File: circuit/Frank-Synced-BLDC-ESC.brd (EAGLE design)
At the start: 49.5 x 25.4 mm, 57 parts, among them IC1 Vreg +5V, Q1 PMOS-DPAK, Q2 NMOS-DPAK, Q4 PMOS-DPAK, Q5 NMOS-DPAK, Q7 PMOS-DPAK, Q8 NMOS-DPAK, U1 ATMEGA168MLF, U2 OSC-16MHz

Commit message: some more fine tunin' traces
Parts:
- moved C2 1.91 mm to (4.45, 20.1)
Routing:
- net N$21: track 0.66 -> 3.42 mm
- net 5V: track 69.7 -> 71.6 mm, vias 6 -> 7
- net GND: vias 24 -> 25
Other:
- board text added: "+5V"

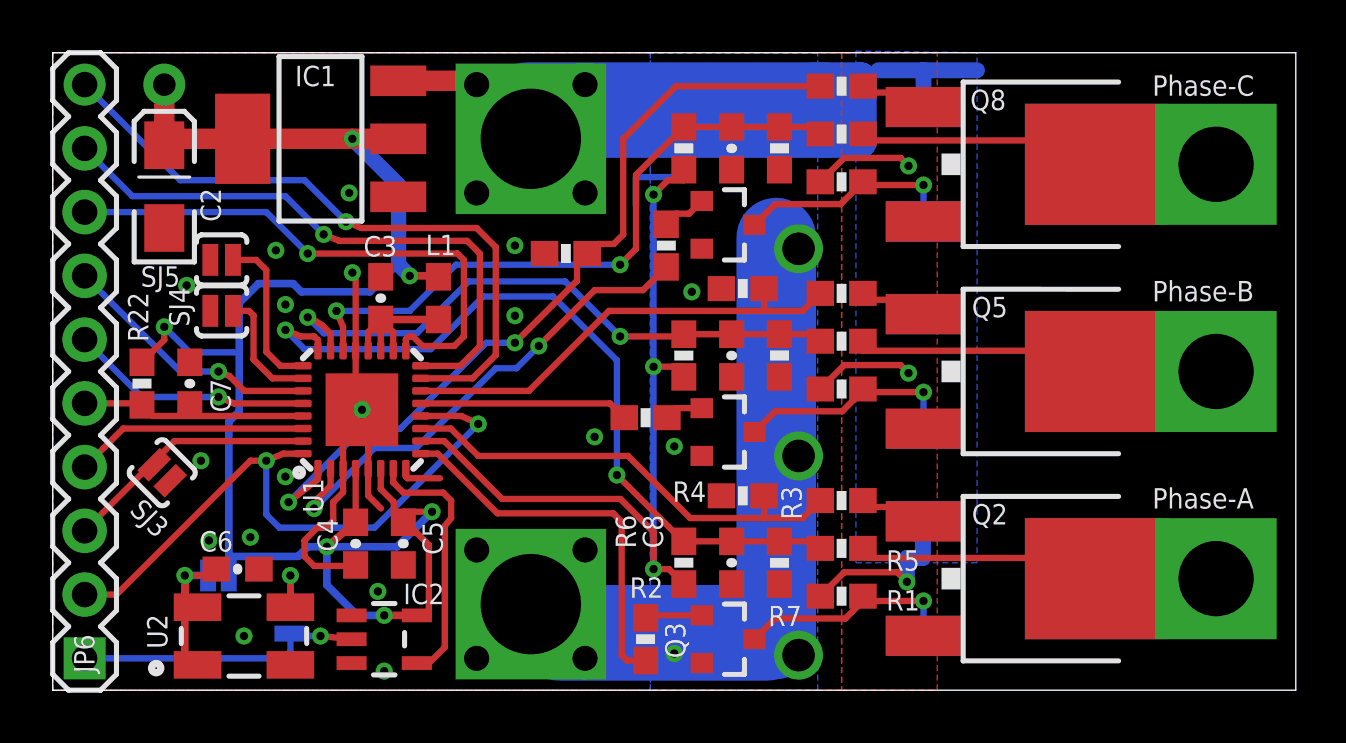
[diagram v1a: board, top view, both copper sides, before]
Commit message: just a bit more shorter, 1.9" now
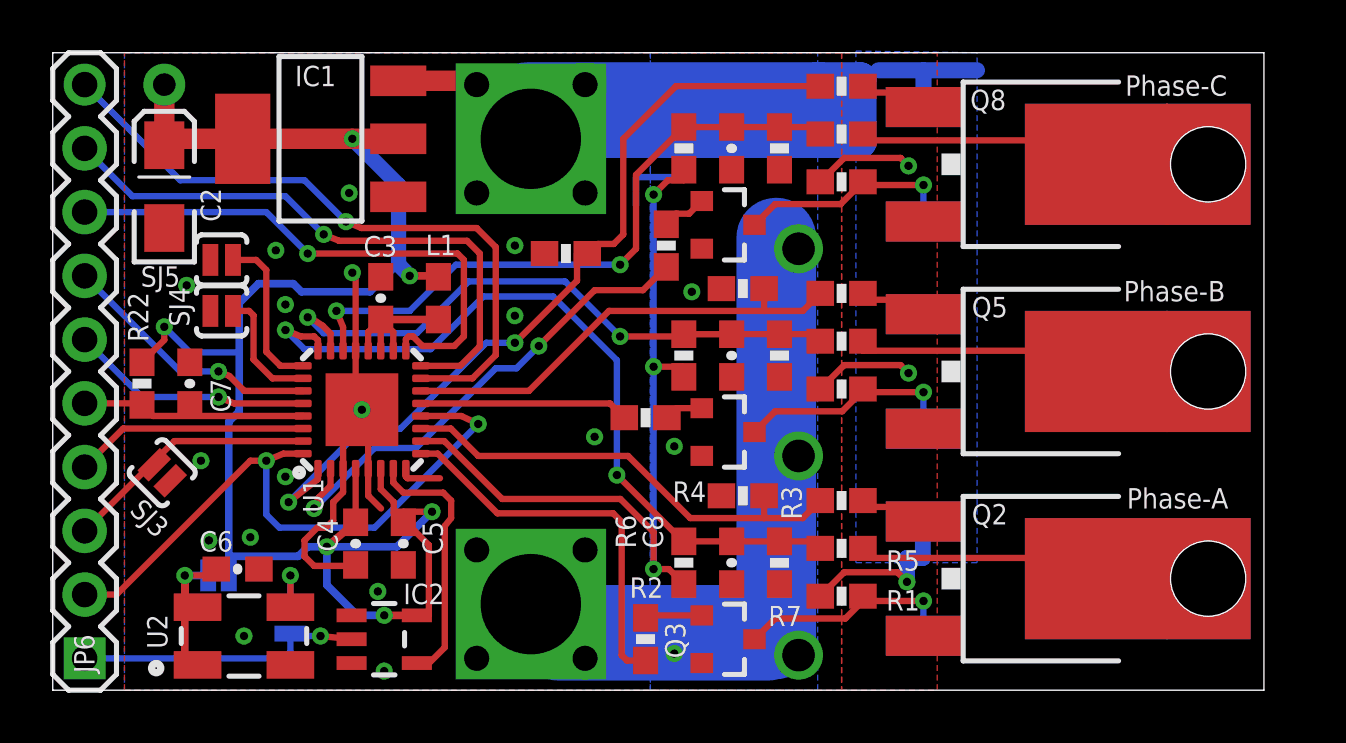
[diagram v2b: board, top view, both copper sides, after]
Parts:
- moved JP1 0.32 mm to (46.0, 4.45), turned to 270 degrees
- moved JP2 0.32 mm to (46.0, 12.7), turned to 270 degrees
- moved JP3 0.32 mm to (46.0, 21.0), turned to 270 degrees
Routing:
- net N$8: track 20.0 -> 19.4 mm
- net N$16: track 19.9 -> 19.3 mm
- net N$1: track 21.0 -> 20.4 mm
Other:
- board size 49.5 x 25.4 mm -> 48.3 x 25.4 mm
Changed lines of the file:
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@@
 <board>
 <plain>
-<wire x1="49.53" y1="0" x2="0" y2="0" width="0" layer="20"/>
+<wire x1="48.26" y1="0" x2="0" y2="0" width="0" layer="20"/>
 <wire x1="0" y1="0" x2="0" y2="25.4" width="0" layer="20"/>
-<wire x1="0" y1="25.4" x2="49.53" y2="25.4" width="0" layer="20"/>
-<wire x1="49.53" y1="25.4" x2="49.53" y2="0" width="0" layer="20"/>
+<wire x1="0" y1="25.4" x2="48.26" y2="25.4" width="0" layer="20"/>
+<wire x1="48.26" y1="25.4" x2="48.26" y2="0" width="0" layer="20"/>
 <rectangle x1="15.24" y1="18.161" x2="22.86" y2="25.4" layer="41"/>
 <rectangle x1="15.24" y1="18.161" x2="22.86" y2="25.4" layer="42" rot="R180"/>
 <wire x1="22.86" y1="20.955" x2="31.115" y2="20.955" width="0.254" layer="42"/>
-<text x="43.815" y="7.239" size="0.8128" layer="25" ratio="10">Phase-A</text>
-<text x="43.815" y="15.494" size="0.8128" layer="25" ratio="10">Phase-B</text>
-<text x="43.815" y="23.6855" size="0.8128" layer="25" ratio="10">Phase-C</text>
-<text x="48.895" y="15.494" size="0.8128" layer="26" ratio="10" rot="MR0">Phase-B</text>
-<text x="48.895" y="7.239" size="0.8128" layer="26" ratio="10" rot="MR0">Phase-A</text>
-<text x="48.8315" y="23.6855" size="0.8128" layer="26" ratio="10" rot="MR0">Phase-C</text>
+<text x="42.799" y="7.239" size="0.8128" layer="25" ratio="10">Phase-A</text>
+<text x="42.672" y="15.494" size="0.8128" layer="25" ratio="10">Phase-B</text>
+<text x="42.7355" y="23.6855" size="0.8128" layer="25" ratio="10">Phase-C</text>
+<text x="47.752" y="15.494" size="0.8128" layer="26" ratio="10" rot="MR0">Phase-B</text>
+<text x="47.879" y="7.239" size="0.8128" layer="26" ratio="10" rot="MR0">Phase-A</text>
+<text x="47.8155" y="23.6855" size="0.8128" layer="26" ratio="10" rot="MR0">Phase-C</text>
 <text x="20.8915" y="7.112" size="0.8128" layer="26" ratio="10" rot="MR0">Batt-Neg</text>
 <text x="21.1455" y="17.8435" size="0.8128" layer="26" ratio="10" rot="MR0">Batt-Pos</text>
@@
 </autorouter>
 <elements>
-<element name="JP1" library="Frank-Synced-BLDC-ESC" package="1X1-MOTOR" value="PHASE-A" x="46.355" y="4.445" smashed="yes" rot="MR90"/>
+<element name="JP1" library="Frank-Synced-BLDC-ESC" package="1X1-MOTOR" value="PHASE-A" x="46.0375" y="4.445" smashed="yes" rot="MR270"/>
 <element name="Q1" library="Frank-Synced-BLDC-ESC" package="DPAK" value="PMOS-DPAK" x="40.005" y="4.445" smashed="yes" rot="MR90">
 <attribute name="NAME" x="36.3665" y="7.112" size="0.8128" layer="26" ratio="10" rot="MR180"/>
@@
 <attribute name="VALUE" x="30.4165" y="6.4135" size="0.4064" layer="27" font="vector"/>
 </element>
-<element name="JP2" library="Frank-Synced-BLDC-ESC" package="1X1-MOTOR" value="PHASE-B" x="46.355" y="12.7" smashed="yes" rot="MR0"/>
+<element name="JP2" library="Frank-Synced-BLDC-ESC" package="1X1-MOTOR" value="PHASE-B" x="46.0375" y="12.7" smashed="yes" rot="MR270"/>
 <element name="Q4" library="Frank-Synced-BLDC-ESC" package="DPAK" value="PMOS-DPAK" x="40.005" y="12.7" smashed="yes" rot="MR90">
 <attribute name="NAME" x="36.43" y="15.4305" size="0.8128" layer="26" ratio="10" rot="MR180"/>
@@
 <attribute name="VALUE" x="30.4165" y="14.6685" size="0.4064" layer="27" font="vector"/>
 </element>
-<element name="JP3" library="Frank-Synced-BLDC-ESC" package="1X1-MOTOR" value="PHASE-C" x="46.355" y="20.955" smashed="yes" rot="MR0"/>
+<element name="JP3" library="Frank-Synced-BLDC-ESC" package="1X1-MOTOR" value="PHASE-C" x="46.0375" y="20.955" smashed="yes" rot="MR270"/>
 <element name="Q7" library="Frank-Synced-BLDC-ESC" package="DPAK" value="PMOS-DPAK" x="40.005" y="20.955" smashed="yes" rot="MR90">
 <attribute name="NAME" x="36.684" y="23.749" size="0.8128" layer="26" ratio="10" rot="MR180"/>
@@
 <contactref element="JP1" pad="P$1"/>
 <contactref element="R5" pad="1"/>
-<wire x1="41.593" y1="4.445" x2="46.355" y2="4.445" width="3.175" layer="1"/>
+<wire x1="41.593" y1="4.445" x2="46.0375" y2="4.445" width="3.175" layer="1"/>
 <contactref element="Q1" pad="4"/>
-<wire x1="41.593" y1="4.445" x2="46.355" y2="4.445" width="3.175" layer="16"/>
+<wire x1="41.593" y1="4.445" x2="46.0375" y2="4.445" width="3.175" layer="16"/>
 <wire x1="32.2825" y1="5.6515" x2="32.2825" y2="5.5245" width="0.254" layer="1"/>
 <wire x1="41.593" y1="5.5245" x2="41.593" y2="4.445" width="0.254" layer="1"/>
@@
 <wire x1="32.6635" y1="5.2705" x2="41.593" y2="5.2705" width="0.254" layer="1"/>
 <wire x1="41.593" y1="5.2705" x2="41.593" y2="4.445" width="0.254" layer="1"/>
+<wire x1="41.593" y1="4.445" x2="41.593" y2="4.445" width="0" layer="19" extent="1-16"/>
 </signal>
 <signal name="+12V">
@@
 <vertex x="23.8125" y="0"/>
 <vertex x="23.8125" y="25.4"/>
-<vertex x="0" y="25.4"/>
-<vertex x="0" y="0"/>
+<vertex x="2.8575" y="25.4"/>
+<vertex x="2.8575" y="0"/>
 </polygon>
 <polygon width="0.254" layer="1" spacing="0.254" isolate="0.254">
-<vertex x="0" y="0"/>
-<vertex x="0" y="25.4"/>
+<vertex x="2.8575" y="0"/>
+<vertex x="2.8575" y="25.4"/>
 <vertex x="31.4325" y="25.4"/>
 <vertex x="31.4325" y="0"/>
@@
 <contactref element="JP2" pad="P$1"/>
 <contactref element="R10" pad="1"/>
-<wire x1="41.593" y1="12.7" x2="46.355" y2="12.7" width="3.175" layer="1"/>
+<wire x1="41.593" y1="12.7" x2="46.0375" y2="12.7" width="3.175" layer="1"/>
 <contactref element="Q4" pad="4"/>
-<wire x1="41.593" y1="12.7" x2="46.355" y2="12.7" width="3.175" layer="16"/>
+<wire x1="41.593" y1="12.7" x2="46.0375" y2="12.7" width="3.175" layer="16"/>
 <wire x1="32.2825" y1="13.9065" x2="32.2825" y2="13.5255" width="0.254" layer="1"/>
 <wire x1="32.2825" y1="13.5255" x2="41.593" y2="13.5255" width="0.254" layer="1"/>
 <wire x1="41.593" y1="13.5255" x2="41.593" y2="12.7" width="0.254" layer="1"/>
+<wire x1="41.593" y1="12.7" x2="41.593" y2="12.7" width="0" layer="19" extent="1-16"/>
 </signal>
 <signal name="N$10">
@@
 <contactref element="JP3" pad="P$1"/>
 <contactref element="R17" pad="1"/>
-<wire x1="41.593" y1="20.955" x2="46.355" y2="20.955" width="3.175" layer="1"/>
+<wire x1="41.593" y1="20.955" x2="46.0375" y2="20.955" width="3.175" layer="1"/>
 <contactref element="Q7" pad="4"/>
-<wire x1="41.593" y1="20.955" x2="46.355" y2="20.955" width="3.175" layer="16"/>
+<wire x1="41.593" y1="20.955" x2="46.0375" y2="20.955" width="3.175" layer="16"/>
 <wire x1="32.2825" y1="22.1615" x2="32.5365" y2="21.9075" width="0.254" layer="1"/>
 <wire x1="32.5365" y1="21.9075" x2="41.5925" y2="21.9075" width="0.254" layer="1"/>
 <wire x1="41.5925" y1="21.9075" x2="41.5925" y2="20.955" width="0.254" layer="1"/>
 <wire x1="41.593" y1="20.955" x2="41.5925" y2="20.955" width="0.254" layer="1"/>
+<wire x1="41.593" y1="20.955" x2="41.593" y2="20.955" width="0" layer="19" extent="1-16"/>
 </signal>
 <signal name="N$17">
@@
 </signal>
 </signals>
-<errors>
-</errors>
 </board>
 </drawing>
